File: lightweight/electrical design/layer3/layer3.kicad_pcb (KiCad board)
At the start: 2 copper layers, 189.7 x 105 mm, 60 parts, among them J1 SH1.0 5P, J10 SH1.0 2P, J11 SH1.0 5P, J2 SH1.0 5P, J3 SH1.0 5P, J5 Conn_01x16_Socket, J6 SH1.0 Female, SW1 SW_SPDT, SW5 SW_Push, U1 TEENSY 4.0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

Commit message: update lw pcbs
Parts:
- added SW2: SW_DPDT_x2, Switches:SWITCH_SPDT_PTH_11.6X4.0MM_LOCK, F.Cu at (136.0, 105.0)
- J10: moved to B.Cu
- moved SW1 47.4 mm to (42.8, 62.6), turned to 0 degrees
- moved J10 16.4 mm to (105.0, 143.6)
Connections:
- C1 pad 2: +3V3 -> /ir/MCU3V3
- C2 pad 2: +3V3 -> /ir/MCU3V3
- C3 pad 2: +3V3 -> /ir/MCU3V3
- FB2 pad 1: +3V3 -> /ir/MCU3V3
- R8 pad 2: +3V3 -> /ir/MCU3V3
- U7 pad 24: +3V3 -> /ir/MCU3V3
- U7 pad 34: /ir/IR18 -> /ir/SWDIO
- U7 pad 36: +3V3 -> /ir/MCU3V3
- U7 pad 37: /ir/IR19 -> /ir/SWDCLOCK
- U7 pad 43: unconnected-(U7-PB7-Pad43) -> /ir/IR19
- U7 pad 45: unconnected-(U7-PB8-Pad45) -> /ir/IR18
- U7 pad 48: +3V3 -> /ir/MCU3V3
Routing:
- net /EN: track 192.2 -> 258.5 mm, vias 7 -> 8
- net /ir/MCU3V3: track 0.00 -> 43.5 mm, vias 0 -> 2
- net +3V3: track 493.2 -> 486.3 mm, vias 5 -> 3
- net /ir/IR18: track 47.6 -> 45.0 mm
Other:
- board size 189.7 x 105 mm -> 188.9 x 115 mm

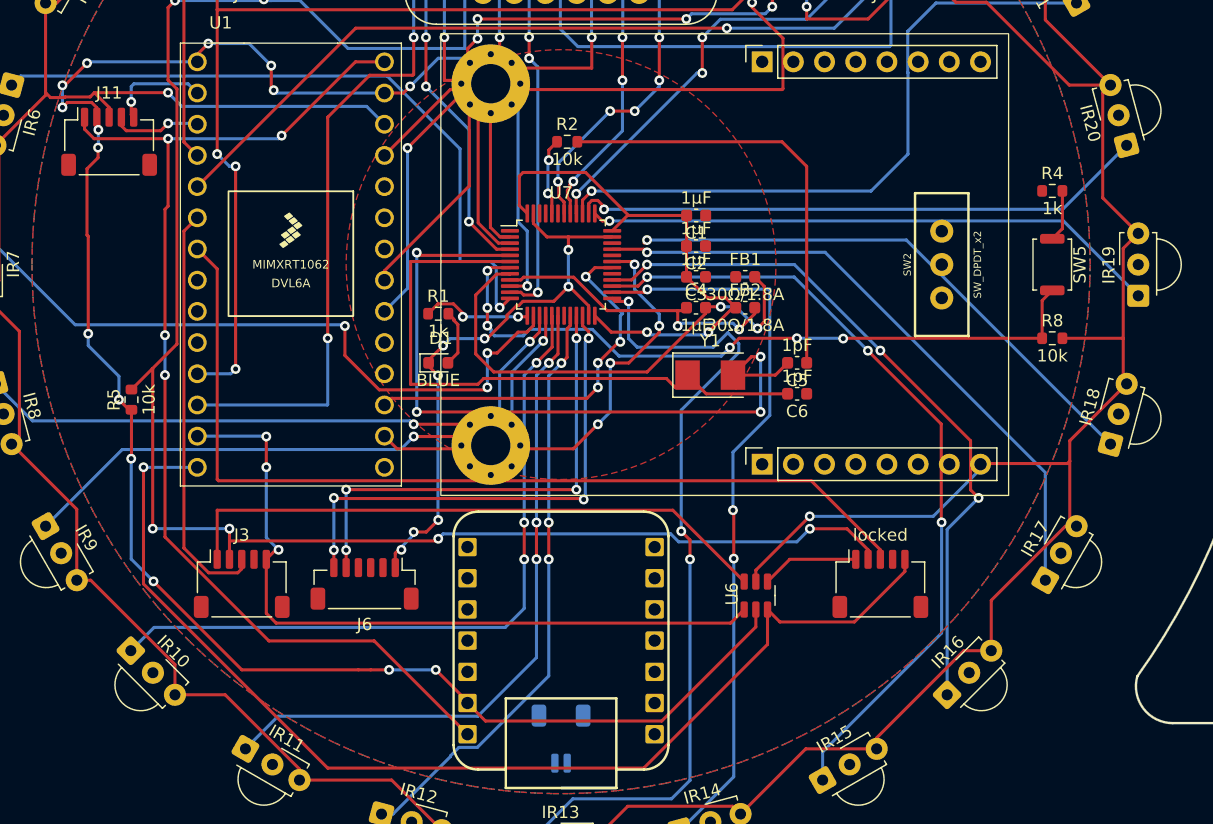
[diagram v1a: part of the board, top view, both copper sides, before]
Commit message: move stuff around layer 3; add stm32 prog switch
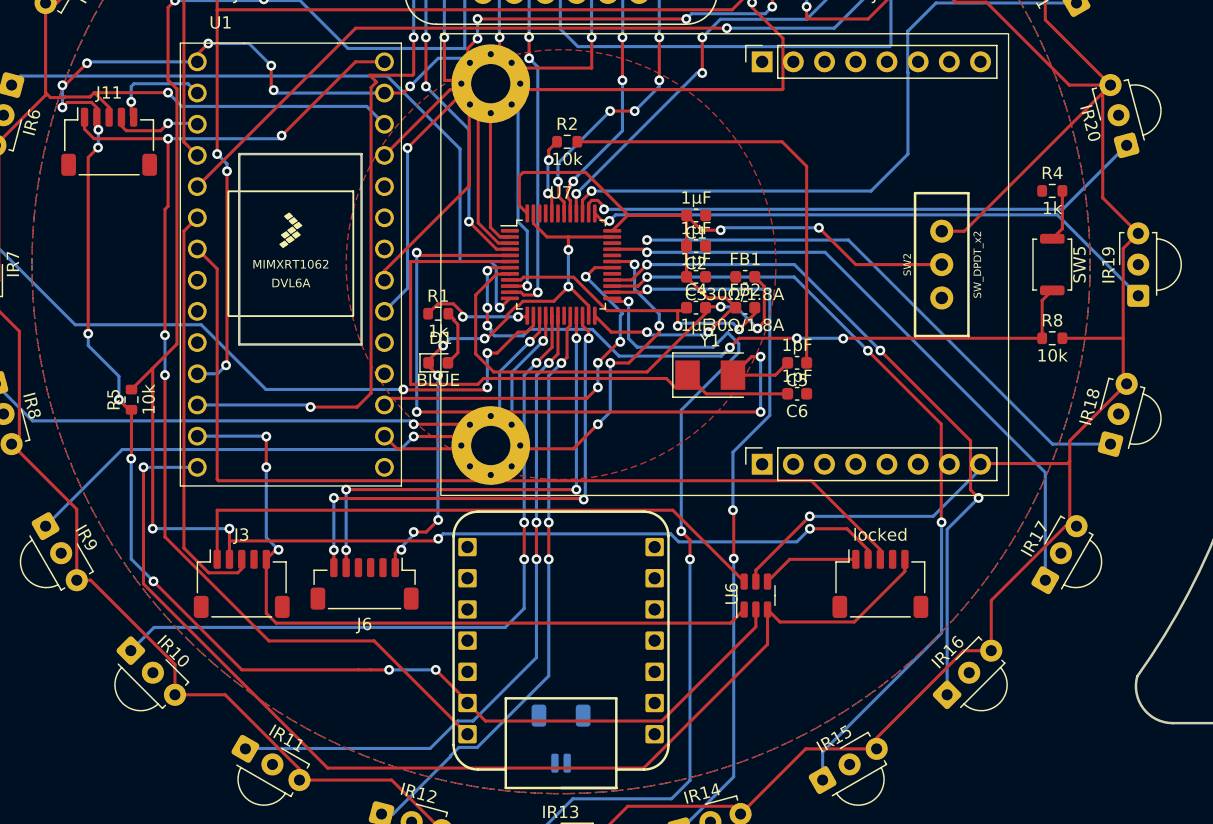
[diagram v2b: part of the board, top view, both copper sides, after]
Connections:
- SW2 pad 3: unconnected-(SW2A-C-Pad3) -> /ir/PROG3V3
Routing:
- net /ir/MCU3V3: track 43.5 -> 66.1 mm, vias 2 -> 4
- net +3V3: track 486.3 -> 504.9 mm
- net /M2INA: track 88.0 -> 90.1 mm
- net /M1INA: track 81.6 -> 80.1 mm
- net /ir/IR7: track 56.0 -> 54.6 mm
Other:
- outline, holes or cut-outs redrawn

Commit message: reposition ir ring
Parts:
- moved IR23 4.48 mm to (130.7, 60.4)
- moved IR9 4.48 mm to (60.4, 130.7)
- moved IR15 4.48 mm to (130.7, 149.6)
- moved IR17 4.48 mm to (149.6, 130.7)
- moved IR3 4.48 mm to (79.3, 60.4)
- moved IR5 4.48 mm to (60.4, 79.3)
- moved IR11 4.48 mm to (79.3, 149.6)
- moved IR21 4.48 mm to (149.6, 79.3)
- moved IR16 4.48 mm to (141.4, 141.4)
- moved IR10 4.48 mm to (68.6, 141.4)
- moved IR22 4.48 mm to (141.4, 68.6)
- moved IR4 4.48 mm to (68.6, 68.6)
- moved IR1 4.48 mm to (105.0, 53.5)
- moved IR7 4.48 mm to (53.5, 105.0)
- moved IR13 4.47 mm to (105.0, 156.5)
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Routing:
- net /ir/IR19: track 47.4 -> 0.00 mm, vias 1 -> 0
- net /ir/IR18: track 45.0 -> 0.00 mm, vias 1 -> 0
- net +3V3: track 504.9 -> 529.1 mm, vias 3 -> 2
- net /ir/MCU3V3: track 66.1 -> 81.6 mm
- net /ir/IR14: track 60.1 -> 65.0 mm
- net /ir/IR3: track 48.5 -> 53.3 mm
- net /ir/IR17: track 51.6 -> 56.4 mm
- net /ir/IR11: track 55.3 -> 60.1 mm
- net /ir/IR5: track 81.5 -> 86.3 mm
- net /ir/IR23: track 51.8 -> 56.6 mm
- net /ir/IR21: track 53.8 -> 58.6 mm
- net /ir/IR15: track 65.1 -> 69.9 mm
- net /ir/IR9: track 52.0 -> 56.8 mm
- net /ir/IR8: track 52.6 -> 57.4 mm
- net /ir/IR24: track 48.1 -> 52.9 mm
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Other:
- outline, holes or cut-outs redrawn
